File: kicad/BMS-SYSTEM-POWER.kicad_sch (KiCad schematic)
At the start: 46 parts, among them Q11 2N3904, Q3 PNP-SOT23, U4 SY8089A, U5 SY8089A, U8 AP63300WU-7

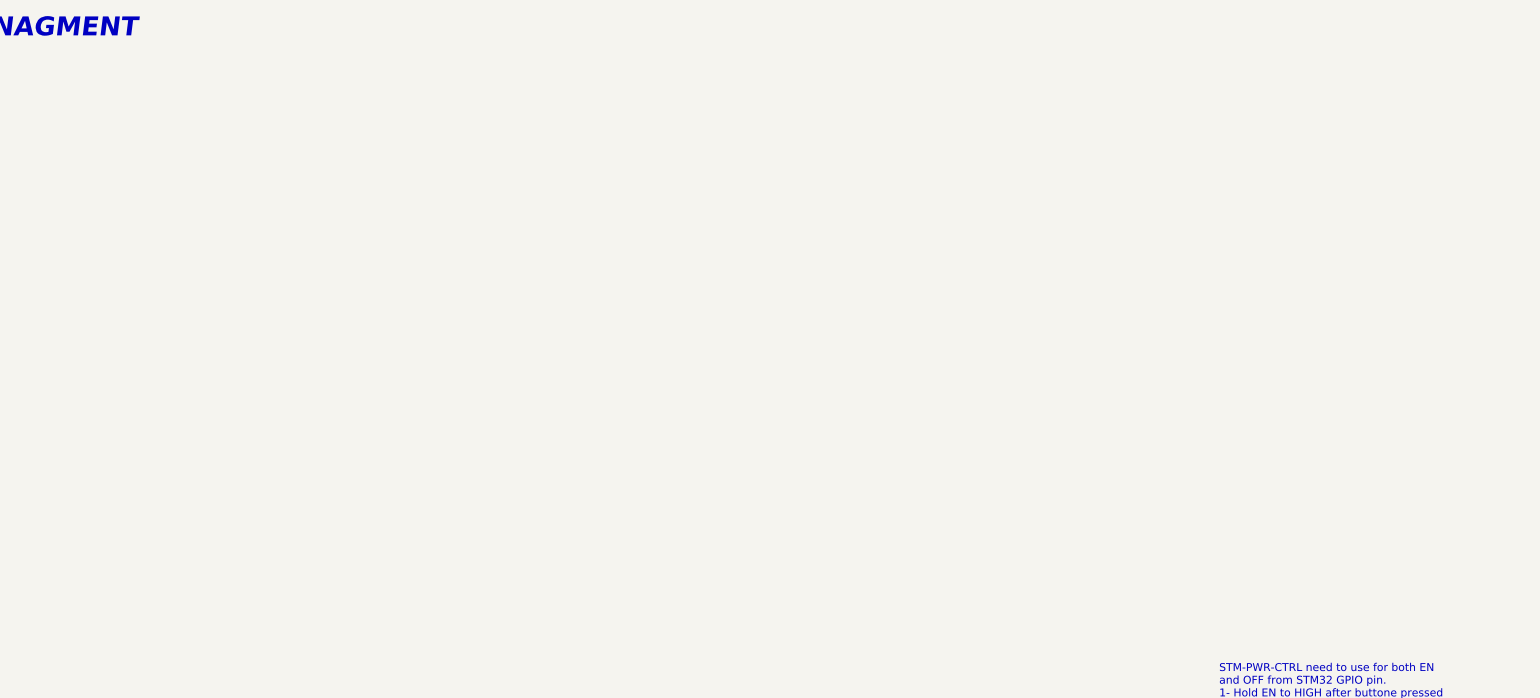
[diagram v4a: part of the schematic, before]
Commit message: RTC clock, signal integrity
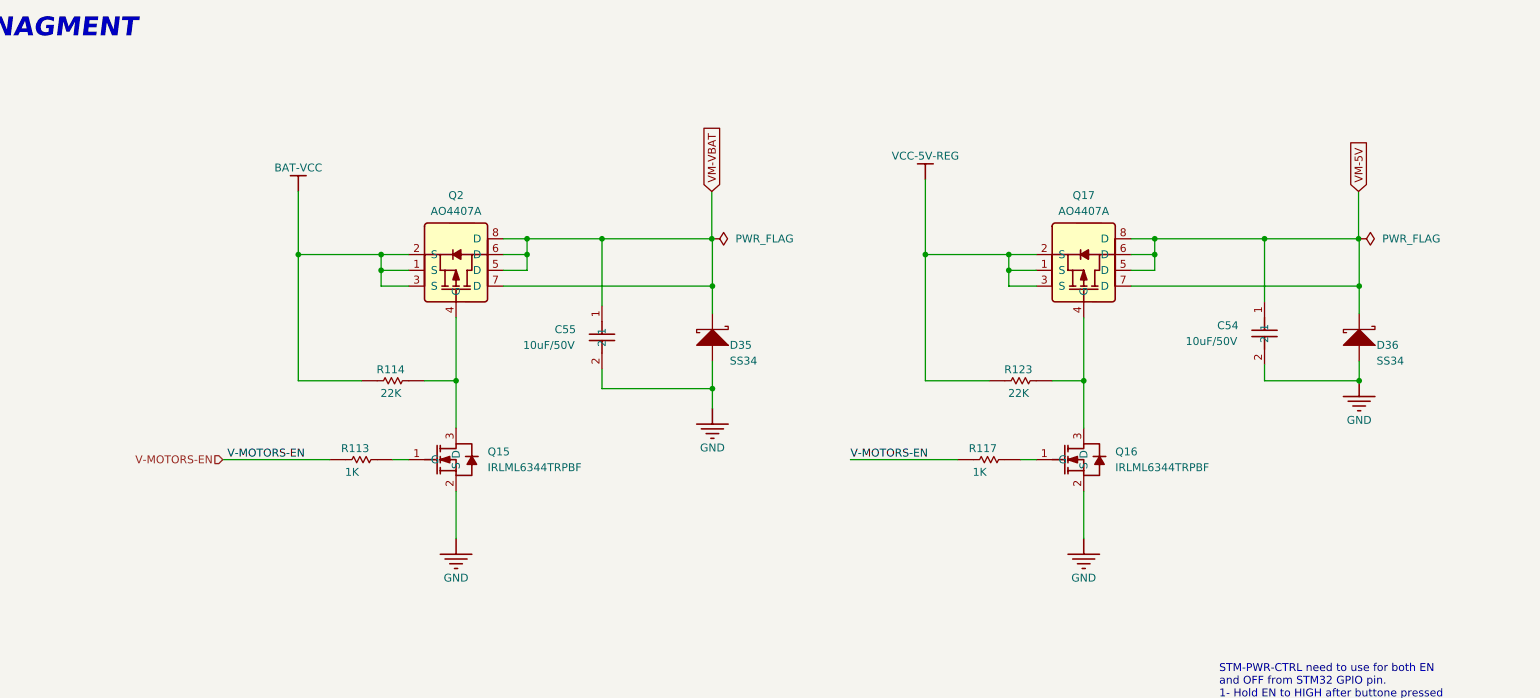
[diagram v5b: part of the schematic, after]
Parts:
- added C54, C55: 10uF/50V, Capacitor_SMD:C_0603_1608Metric, symbol JLCImport:CL21A106KBYQNNE
- added D35, D36: SS34, oomwoo_altium:SMA, symbol DesignLibrary:MAIN-BRUSH MOTOR_1_DIODE-2_DesignLibrary.SchLib
- added Q15, Q16: IRLML6344TRPBF, JLCImport:IRLML6344TRPBF, symbol JLCImport:IRLML6344TRPBF
- added Q17, Q2: AO4407A, JLCImport:AO4407A, symbol JLCImport:AO4407A
- added R113, R117: 1K, Resistor_SMD:R_0603_1608Metric, symbol DesignLibrary:MAIN-FAN_0_Resistor-1_DesignLibrary.SchLib
- added R114, R123: 22K, Resistor_SMD:R_0603_1608Metric, symbol DesignLibrary:MAIN-FAN_0_Resistor-1_DesignLibrary.SchLib
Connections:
- net BAT-VCC: now also Q2.1 (S), Q2.2 (S), Q2.3 (S), R114.1
- net GND: now also C54.2, C55.2, D35.1 (A), D36.1 (A), Q15.2 (S), Q16.2 (S)
- net VCC-5V-REG: now also Q17.1 (S), Q17.2 (S), Q17.3 (S), R123.1
- new net: Q15.3 (D), Q2.4 (G), R114.2
- new net: Q16.1 (G), R117.2
- new net: Q16.3 (D), Q17.4 (G), R123.2
- new net: Q15.1 (G), R113.2
- new net V-MOTORS-EN: R113.1, R117.1
- new net VM-5V: C54.1, D36.2 (K), Q17.5 (D), Q17.6 (D), Q17.7 (D), Q17.8 (D)
- new net VM-VBAT: C55.1, D35.2 (K), Q2.5 (D), Q2.6 (D), Q2.7 (D), Q2.8 (D)

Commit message: External RTC; IR light; side sensors
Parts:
- removed C19, C22: 22uF/10V, Capacitor_SMD:C_0603_1608Metric, symbol DesignLibrary:POWER_1_Capacitor-1_DesignLibrary.SchLib
- removed C20: 100nF/10V, Capacitor_SMD:C_0603_1608Metric, symbol DesignLibrary:POWER_1_Capacitor-1_DesignLibrary.SchLib
- removed C21: 20pF, Capacitor_SMD:C_0603_1608Metric, symbol DesignLibrary:POWER_2_Capacitor-1_DesignLibrary.SchLib
- removed C36: 10uF/50V, Capacitor_SMD:C_0603_1608Metric, symbol JLCImport:CL21A106KBYQNNE
- removed C38, C40: 100nF/50V, Capacitor_SMD:C_0603_1608Metric, symbol Library:C_0603
- removed C42: 47pF/10V, Capacitor_SMD:C_0603_1608Metric, symbol Device:C_Small
- removed C44, C46: 22uF/10V, Capacitor_SMD:C_0805_2012Metric, symbol Device:C_Small
- removed L1: 6.8uH, JLCImport:IHLP2525CZER6R8M01, symbol JLCImport:IHLP2525CZER6R8M01
- removed L4: 2.2uH, oomwoo_altium:IND-SMD_L4.4-W4.2, symbol DesignLibrary:POWER_0_INDUCTOR-SMD_DesignLibrary.SchLib
- removed R11: 100K, Resistor_SMD:R_0603_1608Metric, symbol DesignLibrary:POWER_0_Resistor-1_DesignLibrary.SchLib
- removed R113, R117: 1K, Resistor_SMD:R_0603_1608Metric, symbol DesignLibrary:MAIN-FAN_0_Resistor-1_DesignLibrary.SchLib
- removed R17: 450K, Resistor_SMD:R_0603_1608Metric, symbol DesignLibrary:POWER_2_Resistor-1_DesignLibrary.SchLib
- removed R20: 100K, Resistor_SMD:R_0603_1608Metric, symbol DesignLibrary:POWER_3_Resistor-1_DesignLibrary.SchLib
- removed R42: 158k, Resistor_SMD:R_0603_1608Metric, symbol Device:R_US
- removed R43: 30.1k, Resistor_SMD:R_0603_1608Metric, symbol Device:R_US
- removed U4: SY8089A, oomwoo_altium:SOT5P95B160_300H130, symbol DesignLibrary:POWER_0_SY8089A_0_DesignLibrary.SchLib
- removed U8: AP63300WU-7, JLCImport:AP63300WU-7, symbol JLCImport:AP63300WU-7
- added C102, C107, C111, C117, C118, C119: 100nF/50V, Capacitor_SMD:C_0603_1608Metric, symbol Library:C_0603
- added C106, C113, C114, C115, C116, C121, C122, C95: 10uF/50V, Capacitor_SMD:C_0603_1608Metric, symbol JLCImport:CL21A106KBYQNNE
- added C112, C120: 1.2nF/50V, Capacitor_SMD:C_0603_1608Metric, symbol Library:C_0603
- added C7, C8: VT1A101M0505, JLCImport:VT1A101M0505, symbol JLCImport:VT1A101M0505
- added L2, L3: CYA0630-3_3UH, JLCImport:CYA0630-3_3UH, symbol JLCImport:CYA0630-3_3UH
- added R141, R146: 10, symbol Device:R_US
- added R143, R148: 12k, symbol Device:R_US
- added R144: 69.8k, symbol Device:R_US
- added R145: 22.1k, symbol Device:R_US
- added R147: 20k, symbol Device:R_US
- added R149: 2.2k, symbol Device:R_US
- added U21, U22: AP64501SP-13, JLCImport:AP64501SP-13, symbol JLCImport:AP64501SP-13
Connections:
- net BAT-VCC: now also C27.2, R23.1, U5.4 (IN), C102.1, C106.1, C115.1, C116.1, C117.1, C95.1, U21.2 (VIN), U21.3 (EN), U22.2 (VIN), U22.3 (EN)
- net GND: now also C102.2, C106.2, C107.2, C112.2, C113.2, C114.2, C115.2, C116.2, C117.2, C118.2, C120.2, C121.2, C122.2, C7.2, C8.2, C95.2, R145.1, R149.1, U21.7 (GND), U21.9 (EP), U22.7 (GND), U22.9 (EP)
- net V-MOTORS-EN: now also Q15.1 (G), Q16.1 (G)
- net VCC-3V3-P: now also C113.1, C114.1, C7.1, L2.2, R144.2
- net VCC-5V-REG: now also C121.1, C122.1, C8.1, L3.2, R148.2; no longer C27.2, R23.1, U5.4 (IN)
- new net: C118.1, U22.4 (SS)
- new net: L2.1, R141.2, U21.8 (SW)
- new net: C119.1, R146.1
- new net: C119.2, U22.1 (BST)
- new net: C107.1, U21.4 (SS)
- new net: C111.2, U21.1 (BST)
- new net: R144.1, R145.2, U21.5 (FB)
- new net: R143.2, U21.6 (COMP)
- new net: L3.1, R146.2, U22.8 (SW)
- new net: C112.1, R143.1
- new net: C120.1, R147.1
- new net: C111.1, R141.1
- new net: R148.1, R149.2, U22.5 (FB)
- new net: R147.2, U22.6 (COMP)
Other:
- moved on the sheet: D23, R14
